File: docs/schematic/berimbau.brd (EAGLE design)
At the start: 89.2 x 86 mm, 54 parts, among them IC1 7805TV, IC2 LM386N-1, J1 P2_RPI, Q1 BD140, Q2 BD139, U1 ESP32-DEVKIT-C, U2 LMC6482, U3 APA3541

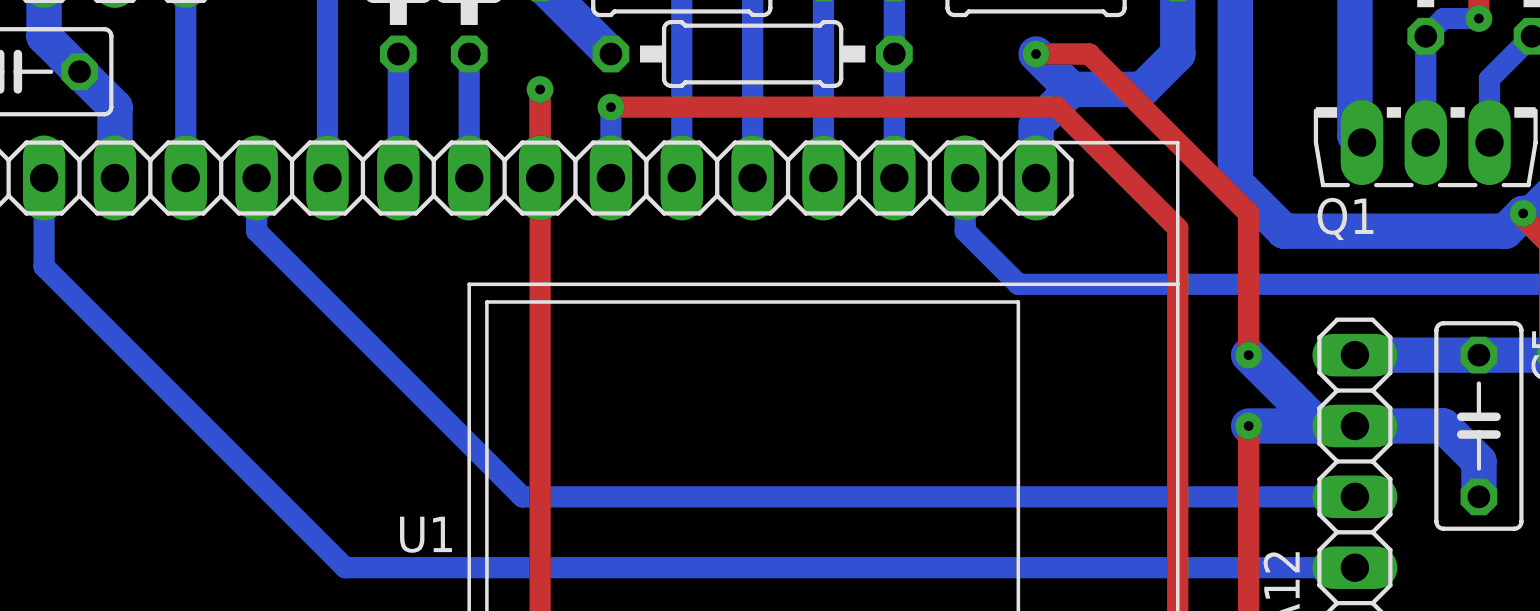
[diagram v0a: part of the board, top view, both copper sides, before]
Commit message: added boot pull-down
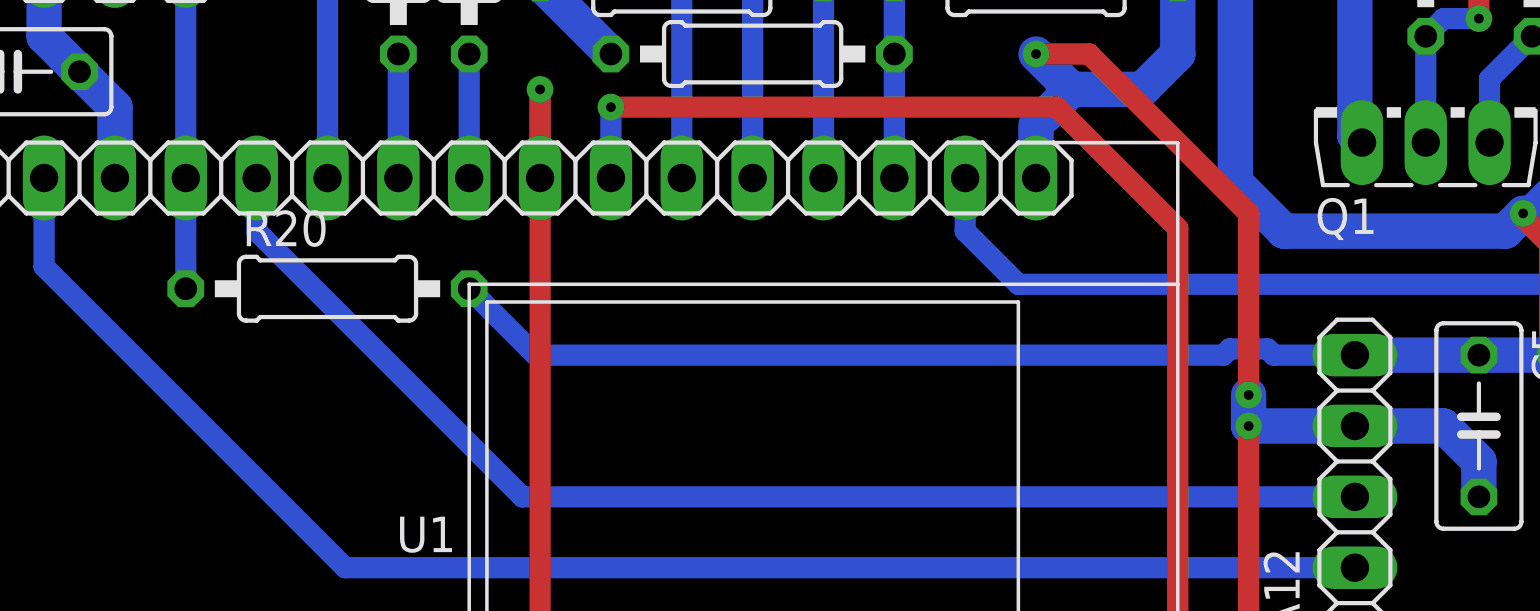
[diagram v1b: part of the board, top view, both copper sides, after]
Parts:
- added R20: 5k2, rcl:0207/10
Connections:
- net GND: now also R20.2
- net URM_TRIGGER: now also R20.1
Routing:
- net GND: track 439.6 -> 472.5 mm
- net URM_TRIGGER: track 7.62 -> 11.6 mm
- net +3V3: track 72.2 -> 69.9 mm
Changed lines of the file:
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@@
 <attribute name="VALUE" x="37.4269" y="50.165" size="1.27" layer="27" ratio="10"/>
+</element>
+<element name="R20" library="rcl" library_urn="urn:adsk.eagle:library:334" package="0207/10" package3d_urn="urn:adsk.eagle:package:23491/2" value="5k2" x="25.0825" y="42.38625" smashed="yes">
+<attribute name="NAME" x="22.0345" y="43.91025" size="1.27" layer="25" ratio="10"/>
+<attribute name="SPICEPREFIX" value="R" x="25.0825" y="42.38625" size="1.778" layer="27" display="off"/>
+<attribute name="VALUE" x="22.8219" y="41.75125" size="1.27" layer="27" ratio="10"/>
 </element>
 </elements>
@@
 <contactref element="A10" pad="4"/>
 <wire x1="20.0025" y1="53.975" x2="20.0025" y2="46.355" width="0.762" layer="16"/>
+<contactref element="R20" pad="1"/>
+<wire x1="20.0025" y1="46.355" x2="20.0025" y2="42.38625" width="0.762" layer="16"/>
 </signal>
 <signal name="LCD_MOSI">
@@
 <via x="31.75" y="63.5" extent="1-16" drill="0.35"/>
 <wire x1="31.75" y1="63.5" x2="26.9875" y2="63.5" width="1.27" layer="1"/>
+<contactref element="R20" pad="2"/>
+<wire x1="30.1625" y1="42.38625" x2="32.54375" y2="40.005" width="0.762" layer="16"/>
+<wire x1="32.54375" y1="40.005" x2="57.19638125" y2="40.005" width="0.762" layer="16"/>
+<wire x1="57.19638125" y1="40.005" x2="57.41863125" y2="40.22725" width="0.762" layer="16"/>
+<wire x1="57.41863125" y1="40.22725" x2="58.78636875" y2="40.22725" width="0.762" layer="16"/>
+<wire x1="58.78636875" y1="40.22725" x2="59.00861875" y2="40.005" width="0.762" layer="16"/>
+<wire x1="59.00861875" y1="40.005" x2="61.9125" y2="40.005" width="0.762" layer="16"/>
 <wire x1="17.78" y1="63.5" x2="14.9225" y2="53.975" width="0" layer="19" extent="16-16"/>
 </signal>
@@
 <wire x1="51.7525" y1="49.53" x2="50.4825" y2="50.8" width="1.27" layer="16"/>
 <via x="50.4825" y="50.8" extent="1-16" drill="0.35"/>
-<wire x1="61.9125" y1="37.465" x2="60.6425" y2="37.465" width="1.27" layer="16"/>
-<wire x1="60.6425" y1="37.465" x2="58.1025" y2="40.005" width="1.27" layer="16"/>
-<via x="58.1025" y="40.005" extent="1-16" drill="0.35"/>
+<wire x1="58.1025" y1="37.465" x2="58.1025" y2="38.57625" width="1.27" layer="16"/>
+<via x="58.1025" y="38.57625" extent="1-16" drill="0.35"/>
 <wire x1="50.4825" y1="50.8" x2="52.3875" y2="50.8" width="0.762" layer="1"/>
 <wire x1="52.3875" y1="50.8" x2="58.1025" y2="45.085" width="0.762" layer="1"/>
-<wire x1="58.1025" y1="45.085" x2="58.1025" y2="40.005" width="0.762" layer="1"/>
+<wire x1="58.1025" y1="45.085" x2="58.1025" y2="38.57625" width="0.762" layer="1"/>
 <wire x1="55.5625" y1="53.34" x2="55.5625" y2="50.8" width="1.27" layer="16"/>
 </signal>

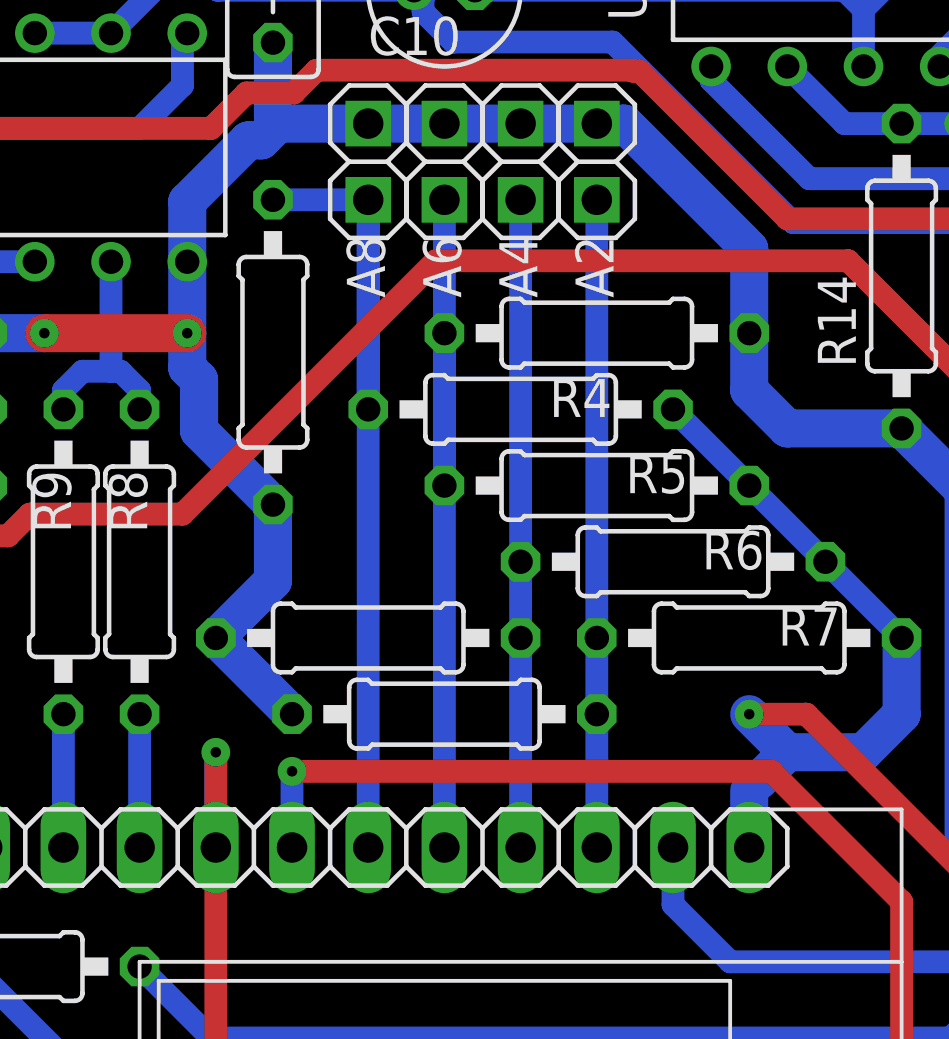
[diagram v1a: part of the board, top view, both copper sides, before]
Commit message: removed pull down on piezo
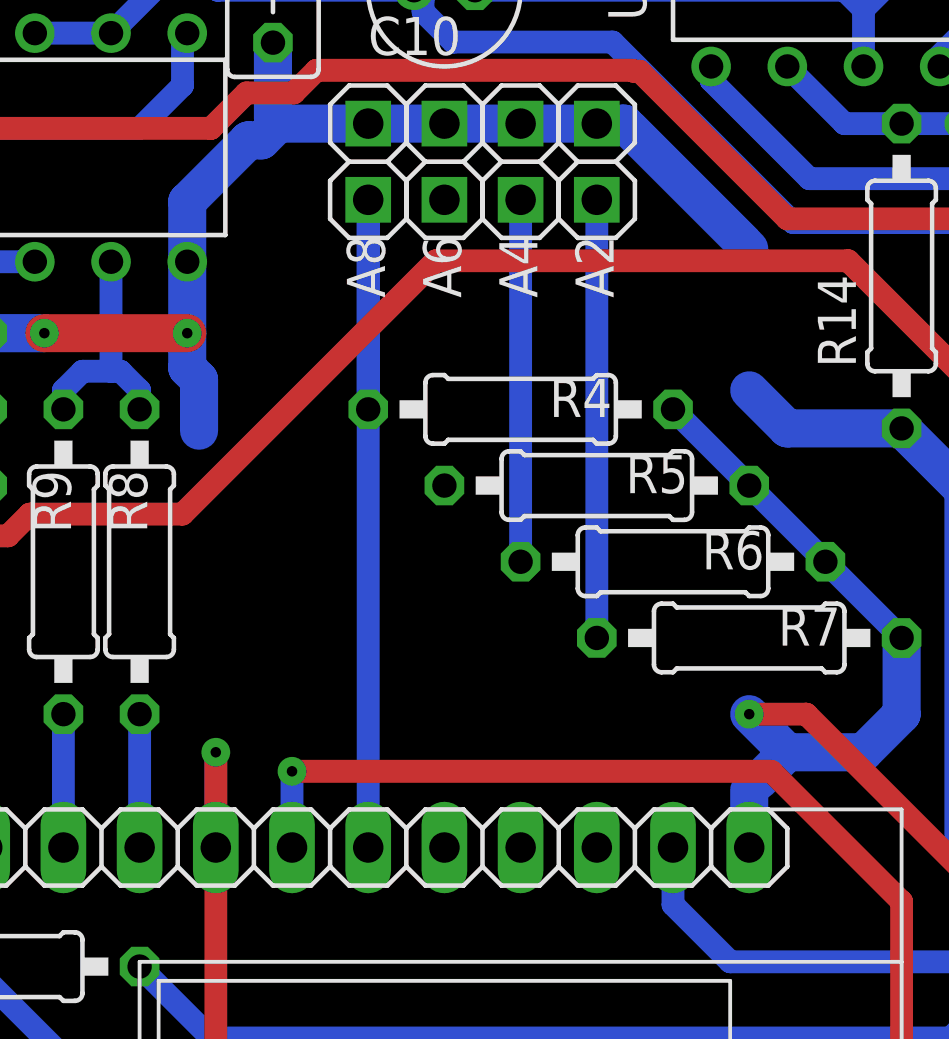
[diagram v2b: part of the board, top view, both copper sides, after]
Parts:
- removed R16, R17, R18, R19: 100R, rcl:0207/10
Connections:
- net B_CAXIXI: no longer R19.1
- net B_MOEDA: no longer R18.1
- net B_PRESA: no longer R17.1
- net B_SOLTA: no longer R16.1
- net GND: no longer R16.2, R17.2, R18.2, R19.2
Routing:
- net B_PRESA: track 26.7 -> 0.00 mm
- net GND: track 472.5 -> 455.4 mm
- net B_MOEDA: track 21.6 -> 12.1 mm
- net B_CAXIXI: track 21.6 -> 14.6 mm
- net B_SOLTA: track 31.7 -> 28.6 mm
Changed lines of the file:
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@@
 <?xml version="1.0" encoding="utf-8"?>
 <!DOCTYPE eagle SYSTEM "eagle.dtd">
-<eagle version="9.3.1">
+<eagle version="9.4.0">
 <drawing>
 <settings>
@@
 <attribute name="VALUE" x="49.4665" y="75.565" size="1.27" layer="27" ratio="10"/>
 </element>
-<element name="R16" library="rcl" library_urn="urn:adsk.eagle:library:334" package="0207/10" package3d_urn="urn:adsk.eagle:package:23491/2" value="100R" x="34.6075" y="62.865" smashed="yes" rot="R270">
-<attribute name="NAME" x="36.1315" y="64.643" size="1.27" layer="25" ratio="10" rot="R270" display="off"/>
-<attribute name="SPICEPREFIX" value="R" x="34.6075" y="62.865" size="1.778" layer="27" rot="R270" display="off"/>
-<attribute name="VALUE" x="35.2425" y="59.9694" size="1.27" layer="27" ratio="10" rot="R90"/>
-</element>
-<element name="R17" library="rcl" library_urn="urn:adsk.eagle:library:334" package="0207/10" package3d_urn="urn:adsk.eagle:package:23491/2" value="100R" x="45.4025" y="63.5" smashed="yes">
-<attribute name="NAME" x="42.3545" y="65.024" size="1.27" layer="25" ratio="10" display="off"/>
-<attribute name="SPICEPREFIX" value="R" x="45.4025" y="63.5" size="1.778" layer="27" display="off"/>
-<attribute name="VALUE" x="48.2981" y="64.135" size="1.27" layer="27" ratio="10" rot="R180"/>
-</element>
-<element name="R18" library="rcl" library_urn="urn:adsk.eagle:library:334" package="0207/10" package3d_urn="urn:adsk.eagle:package:23491/2" value="100R" x="37.7825" y="53.34" smashed="yes" rot="R180">
-<attribute name="NAME" x="40.8305" y="51.816" size="1.27" layer="25" ratio="10" rot="R180" display="off"/>
-<attribute name="SPICEPREFIX" value="R" x="37.7825" y="53.34" size="1.778" layer="27" rot="R180" display="off"/>
-<attribute name="VALUE" x="34.8869" y="52.705" size="1.27" layer="27" ratio="10"/>
-</element>
-<element name="R19" library="rcl" library_urn="urn:adsk.eagle:library:334" package="0207/10" package3d_urn="urn:adsk.eagle:package:23491/2" value="100R" x="40.3225" y="50.8" smashed="yes" rot="R180">
-<attribute name="NAME" x="43.3705" y="49.276" size="1.27" layer="25" ratio="10" rot="R180" display="off"/>
-<attribute name="SPICEPREFIX" value="R" x="40.3225" y="50.8" size="1.778" layer="27" rot="R180" display="off"/>
-<attribute name="VALUE" x="37.4269" y="50.165" size="1.27" layer="27" ratio="10"/>
-</element>
 <element name="R20" library="rcl" library_urn="urn:adsk.eagle:library:334" package="0207/10" package3d_urn="urn:adsk.eagle:package:23491/2" value="5k2" x="25.0825" y="42.38625" smashed="yes">
 <attribute name="NAME" x="22.0345" y="43.91025" size="1.27" layer="25" ratio="10"/>
@@
 <contactref element="R6" pad="2"/>
 <contactref element="A4" pad="2"/>
-<contactref element="R18" pad="1"/>
 <wire x1="42.8625" y1="67.945" x2="42.8625" y2="55.88" width="0.762" layer="16"/>
-<wire x1="42.8625" y1="46.355" x2="42.8625" y2="53.34" width="0.762" layer="16"/>
-<wire x1="42.8625" y1="55.88" x2="42.8625" y2="53.34" width="0.762" layer="16"/>
+<wire x1="42.8625" y1="46.355" x2="42.8625" y2="55.88" width="0" layer="19" extent="1-1"/>
 </signal>
 <signal name="B_CAXIXI">
@@
 <contactref element="R7" pad="2"/>
 <contactref element="A2" pad="2"/>
-<contactref element="R19" pad="1"/>
 <wire x1="45.4025" y1="67.945" x2="45.4025" y2="53.34" width="0.762" layer="16"/>
-<wire x1="45.4025" y1="46.355" x2="45.4025" y2="50.8" width="0.762" layer="16"/>
-<wire x1="45.4025" y1="50.8" x2="45.4025" y2="53.34" width="0.762" layer="16"/>
+<wire x1="45.4025" y1="46.355" x2="45.4025" y2="53.34" width="0" layer="19" extent="1-1"/>
 </signal>
 <signal name="DAC_MSB">
@@
 <contactref element="R5" pad="2"/>
 <contactref element="A6" pad="2"/>
-<contactref element="R17" pad="1"/>
-<wire x1="40.3225" y1="63.5" x2="40.3225" y2="46.355" width="0.762" layer="16"/>
-<wire x1="40.3225" y1="58.42" x2="40.3225" y2="63.5" width="0.762" layer="16"/>
-<wire x1="40.3225" y1="63.5" x2="40.3225" y2="67.945" width="0.762" layer="16"/>
+<wire x1="40.3225" y1="58.42" x2="40.3225" y2="67.945" width="0" layer="19" extent="1-1"/>
+<wire x1="40.3225" y1="46.355" x2="40.3225" y2="58.42" width="0" layer="19" extent="1-1"/>
 </signal>
 <signal name="B_SOLTA">
@@
 <contactref element="R4" pad="2"/>
 <contactref element="A8" pad="2"/>
-<contactref element="R16" pad="1"/>
 <wire x1="37.7825" y1="67.945" x2="37.7825" y2="46.355" width="0.762" layer="16"/>
-<wire x1="34.6075" y1="67.945" x2="37.7825" y2="67.945" width="0.762" layer="16"/>
 <wire x1="37.7825" y1="60.96" x2="37.7825" y2="67.945" width="0.762" layer="16"/>
 </signal>
@@
 <contactref element="A6" pad="1"/>
 <contactref element="A8" pad="1"/>
-<contactref element="R16" pad="2"/>
-<contactref element="R17" pad="2"/>
-<contactref element="R18" pad="2"/>
-<contactref element="R19" pad="2"/>
 <wire x1="17.4625" y1="48.895" x2="17.4625" y2="46.355" width="1.27" layer="16"/>
 <wire x1="16.1925" y1="50.165" x2="17.4625" y2="48.895" width="1.27" layer="16"/>
@@
 <wire x1="55.5625" y1="60.325" x2="51.7525" y2="60.325" width="1.27" layer="16"/>
 <wire x1="51.7525" y1="60.325" x2="50.4825" y2="61.595" width="1.27" layer="16"/>
-<wire x1="50.4825" y1="61.595" x2="50.4825" y2="63.5" width="1.27" layer="16"/>
-<wire x1="50.4825" y1="63.5" x2="50.4825" y2="66.31579375" width="1.27" layer="16"/>
 <wire x1="46.31329375" y1="70.485" x2="45.4025" y2="70.485" width="1.27" layer="16"/>
 <wire x1="50.4825" y1="66.31579375" x2="46.31329375" y2="70.485" width="1.27" layer="16"/>
@@
 <wire x1="40.3225" y1="70.485" x2="37.7825" y2="70.485" width="1.27" layer="16"/>
 <wire x1="34.77670625" y1="70.485" x2="37.7825" y2="70.485" width="1.27" layer="16"/>
-<wire x1="34.6075" y1="57.785" x2="34.6075" y2="55.245" width="1.27" layer="16"/>
-<wire x1="34.6075" y1="55.245" x2="32.7025" y2="53.34" width="1.27" layer="16"/>
-<wire x1="32.7025" y1="53.34" x2="35.2425" y2="50.8" width="1.27" layer="16"/>
 <wire x1="70.1675" y1="64.77" x2="70.1675" y2="67.945" width="1.27" layer="16"/>
 <wire x1="70.1675" y1="67.945" x2="70.1675" y2="70.485" width="1.27" layer="16"/>
@@
 <vertex x="0.3175" y="0"/>
 </polygon>
-<wire x1="32.1437" y1="60.2488" x2="34.6075" y2="57.785" width="1.27" layer="16"/>
 <wire x1="14.9225" y1="66.3575" x2="17.78" y2="63.5" width="1.27" layer="16"/>
 <wire x1="34.6075" y1="73.18375" x2="34.6075" y2="70.65420625" width="1.27" layer="16"/>
@@
 <wire x1="58.78636875" y1="40.22725" x2="59.00861875" y2="40.005" width="0.762" layer="16"/>
 <wire x1="59.00861875" y1="40.005" x2="61.9125" y2="40.005" width="0.762" layer="16"/>
-<wire x1="17.78" y1="63.5" x2="14.9225" y2="53.975" width="0" layer="19" extent="16-16"/>
+<wire x1="50.4825" y1="61.595" x2="50.4825" y2="66.31579375" width="0" layer="19" extent="16-16"/>
+<wire x1="14.9225" y1="53.975" x2="17.78" y2="63.5" width="0" layer="19" extent="16-16"/>
 </signal>
 <signal name="B_BLUE">
